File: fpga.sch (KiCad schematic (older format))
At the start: 1 part, among them U1 LFXP2-xE-xTN144x

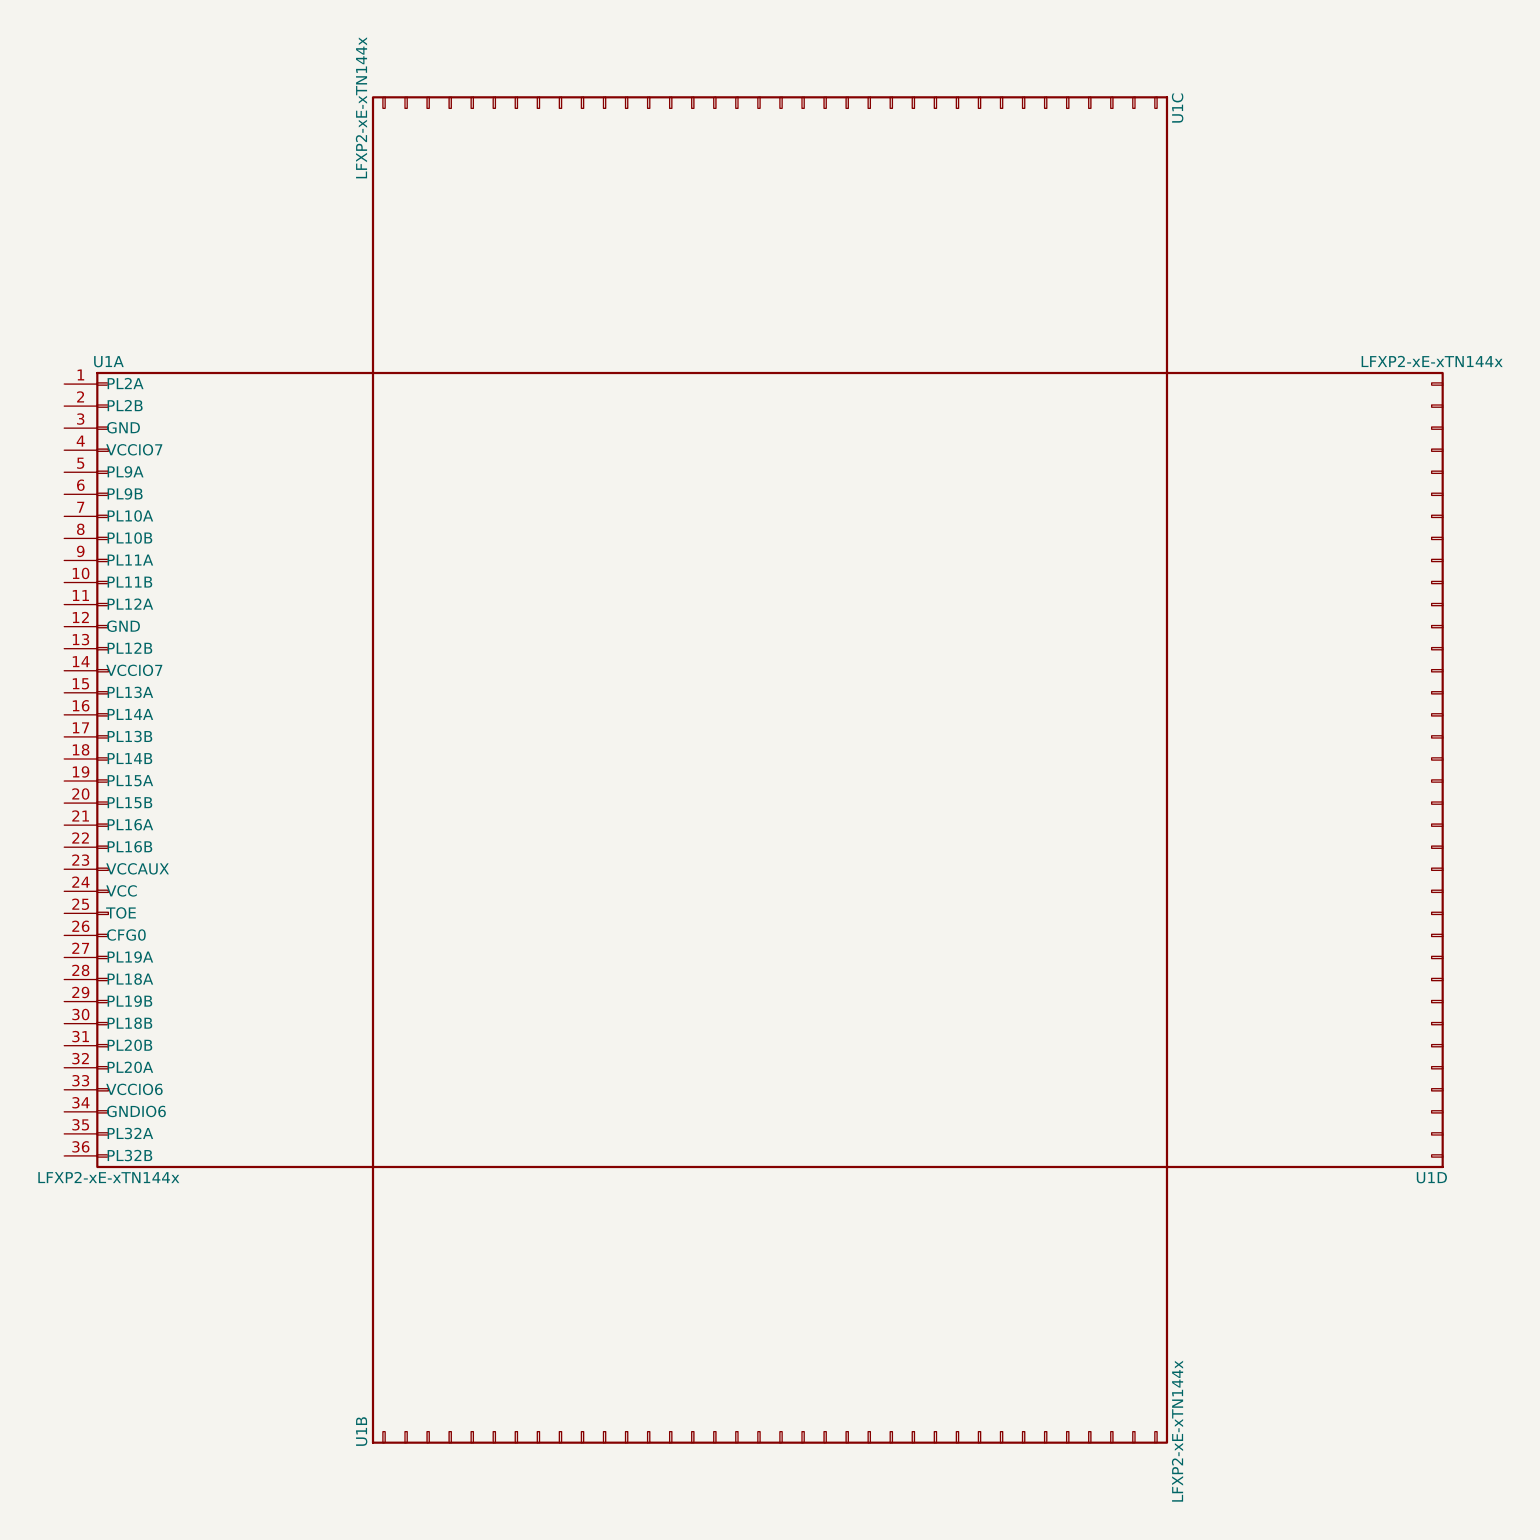
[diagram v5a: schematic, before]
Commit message: footprint: pins on individual units, not common to all
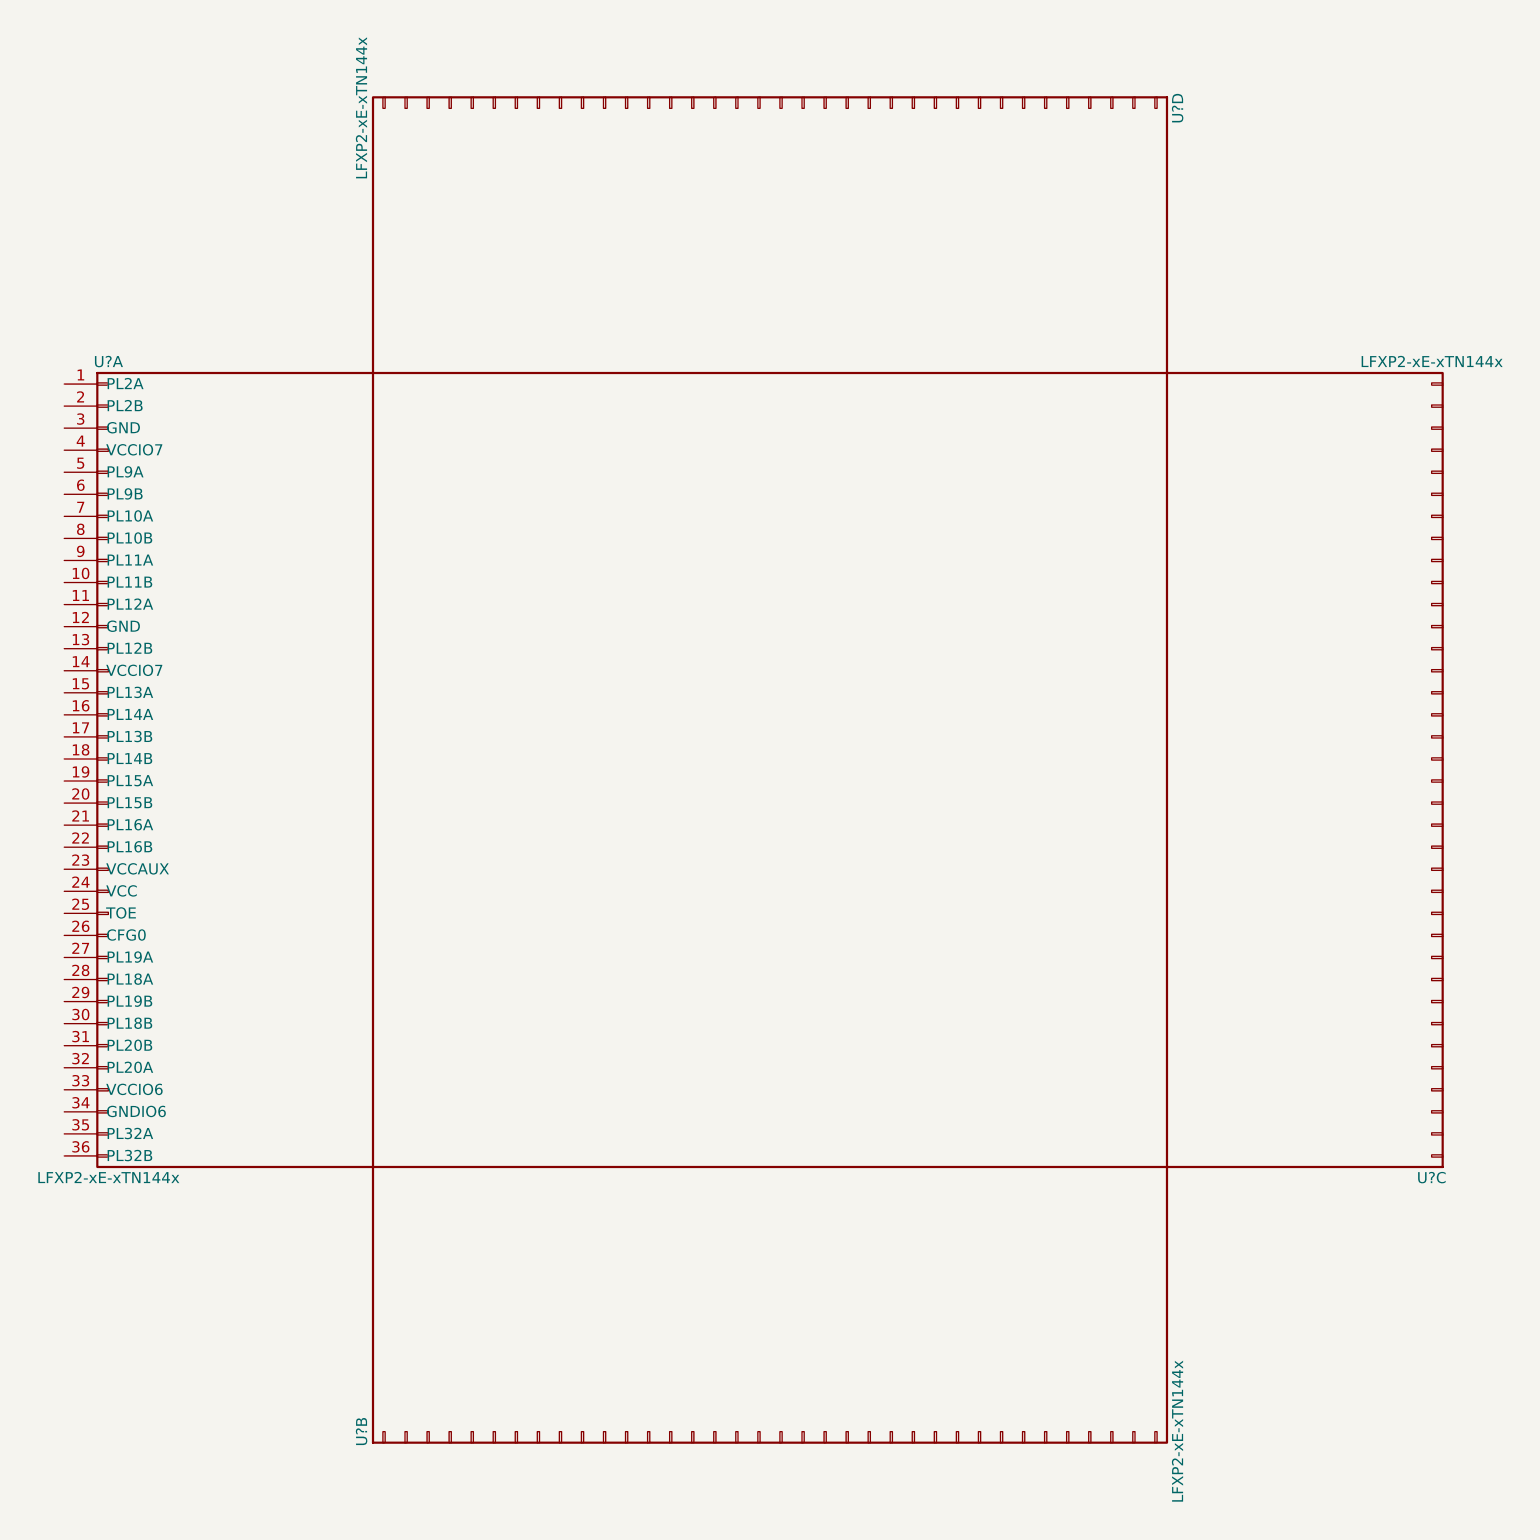
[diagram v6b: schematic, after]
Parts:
- removed U1: LFXP2-xE-xTN144x, Housings_QFP:TQFP-144_20x20mm_Pitch0.5mm, symbol LFXP2-xE-xTN144x
- added U? (x4): LFXP2-xE-xTN144x, symbol LFXP2-xE-xTN144x
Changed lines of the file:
@@
 EESchema Schematic File Version 2
+LIBS:ulx2s-rescue
 LIBS:power
 LIBS:device
@@
 $EndDescr
 $Comp
-L LFXP2-xE-xTN144x U1
-U 1 1 5A13EEFB
+L LFXP2-xE-xTN144x U?
+U 1 1 5A13E2F6
 P 1400 4050
-F 0 "U1" H 1400 5850 50  0000 C CNN
+F 0 "U?" H 1400 5850 50  0000 C CNN
 F 1 "LFXP2-xE-xTN144x" H 1400 2150 50  0000 C CNN
-F 2 "Housings_QFP:TQFP-144_20x20mm_Pitch0.5mm" H 1400 4050 50  0001 C CNN
-F 3 "http://www.latticesemi.com/~/media/LatticeSemi/Documents/DataSheets/LatticeXP2/LatticeXP2FamilyDataSheet.pdf" H 1400 4050 50  0001 C CNN
-F 4 "www.mouser.com" H 1400 4050 60  0001 C CNN "Distributor1_URL"
+F 2 "" H 1400 4050 50  0001 C CNN
+F 3 "" H 1400 4050 50  0001 C CNN
 	1    1400 4050
 	1    0    0    -1
 $EndComp
 $Comp
-L LFXP2-xE-xTN144x U1
-U 2 1 5A13EF4C
+L LFXP2-xE-xTN144x U?
+U 2 1 5A13E3EB
 P 4350 7100
-F 0 "U1" H 4350 8900 50  0000 C CNN
+F 0 "U?" H 4350 8900 50  0000 C CNN
 F 1 "LFXP2-xE-xTN144x" H 4350 5200 50  0000 C CNN
-F 2 "Housings_QFP:TQFP-144_20x20mm_Pitch0.5mm" H 4350 7100 50  0001 C CNN
+F 2 "" H 4350 7100 50  0001 C CNN
 F 3 "" H 4350 7100 50  0001 C CNN
 	2    4350 7100
@@
 $EndComp
 $Comp
-L LFXP2-xE-xTN144x U1
-U 4 1 5A13EF95
+L LFXP2-xE-xTN144x U?
+U 3 1 5A13E576
 P 7400 4150
-F 0 "U1" H 7400 5950 50  0000 C CNN
+F 0 "U?" H 7400 5950 50  0000 C CNN
 F 1 "LFXP2-xE-xTN144x" H 7400 2250 50  0000 C CNN
-F 2 "Housings_QFP:TQFP-144_20x20mm_Pitch0.5mm" H 7400 4150 50  0001 C CNN
+F 2 "" H 7400 4150 50  0001 C CNN
 F 3 "" H 7400 4150 50  0001 C CNN
-	4    7400 4150
+	3    7400 4150
 	-1   0    0    1
 $EndComp
 $Comp
-L LFXP2-xE-xTN144x U1
-U 3 1 5A13EFE6
+L LFXP2-xE-xTN144x U?
+U 4 1 5A13E5E5
 P 4450 1100
-F 0 "U1" H 4450 2900 50  0000 C CNN
+F 0 "U?" H 4450 2900 50  0000 C CNN
 F 1 "LFXP2-xE-xTN144x" H 4450 -800 50  0000 C CNN
-F 2 "Housings_QFP:TQFP-144_20x20mm_Pitch0.5mm" H 4450 1100 50  0001 C CNN
+F 2 "" H 4450 1100 50  0001 C CNN
 F 3 "" H 4450 1100 50  0001 C CNN
-	3    4450 1100
+	4    4450 1100
 	0    1    1    0
 $EndComp
